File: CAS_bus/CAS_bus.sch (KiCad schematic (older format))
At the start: 2 parts

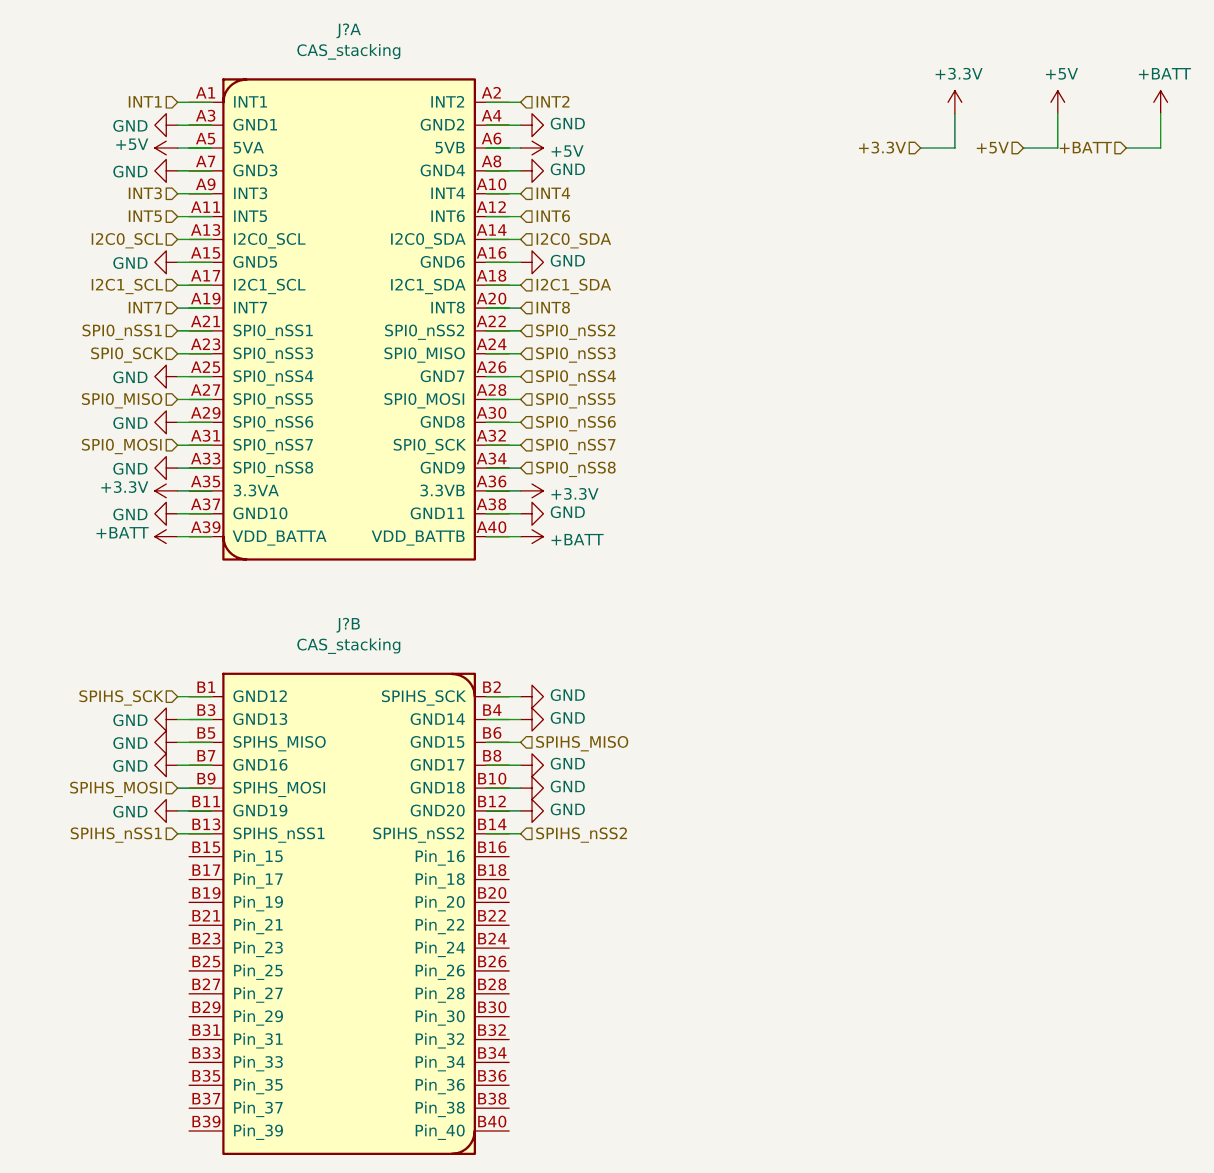
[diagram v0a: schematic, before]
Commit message: flip both connectors to match spreadsheet, and add pin names
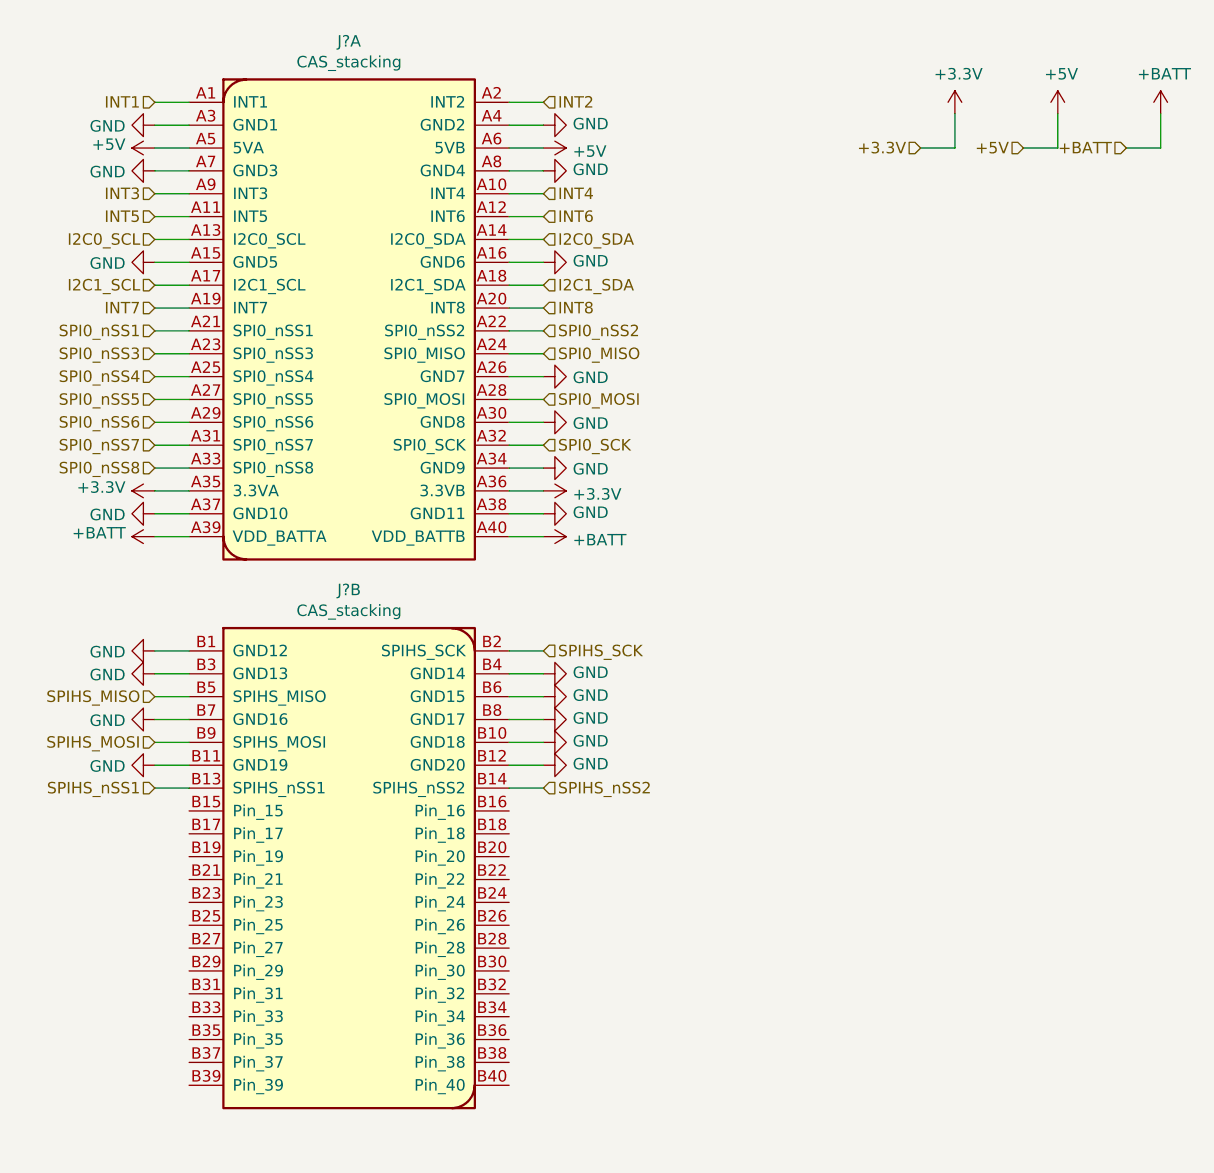
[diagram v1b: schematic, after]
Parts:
- removed J? (x2): CAS_stacking, symbol star-common-lib:CAS_stacking
- added J? (x2): CAS_stacking, symbol star-sch-block-symbols:CAS_stacking

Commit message: fix spelling error
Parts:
- removed J? (x2): CAS_stacking, symbol star-sch-block-symbols:CAS_stacking
- added J? (x2): CAS_stacking, symbol star-sch-block-symbols:CAS_stacking
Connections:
- net +3V3: now also J?.A35 (3.3VA), J?.A36 (3.3VB)
- net +5V: now also J?.A5 (5VA), J?.A6 (5VB)
- net +BATT: now also J?.A39 (VDD_BATTA), J?.A40 (VDD_BATTB)
- net GND: now also J?.A15 (GND5), J?.A16 (GND6), J?.A26 (GND7), J?.A3 (GND1), J?.A30 (GND8), J?.A34 (GND9), J?.A37 (GND10), J?.A38 (GND11), J?.A4 (GND2), J?.A7 (GND3), J?.A8 (GND4), J?.B1 (GND12), J?.B10 (GND18), J?.B11 (GND19), J?.B12 (GND20), J?.B3 (GND13), J?.B4 (GND14), J?.B6 (GND15), J?.B7 (GND16), J?.B8 (GND17)
- net I2C0_SCL: now also J?.A13 (I2C0_SCL)
- net I2C0_SDA: now also J?.A14 (I2C0_SDA)
- net I2C1_SCL: now also J?.A17 (I2C1_SCL)
- net I2C1_SDA: now also J?.A18 (I2C1_SDA)
- net INT1: now also J?.A1 (INT1)
- net INT2: now also J?.A2 (INT2)
- net INT3: now also J?.A9 (INT3)
- net INT4: now also J?.A10 (INT4)
- net INT5: now also J?.A11 (INT5)
- net INT6: now also J?.A12 (INT6)
- net INT7: now also J?.A19 (INT7)
- net INT8: now also J?.A20 (INT8)
- net SPI0_MISO: now also J?.A24 (SPI0_MISO)
- net SPI0_MOSI: now also J?.A28 (SPI0_MOSI)
- net SPI0_SCK: now also J?.A32 (SPI0_SCK)
- net SPI0_nSS1: now also J?.A21 (SPI0_nSS1)
- net SPI0_nSS2: now also J?.A22 (SPI0_nSS2)
- net SPI0_nSS3: now also J?.A23 (SPI0_nSS3)
- net SPI0_nSS4: now also J?.A25 (SPI0_nSS4)
- net SPI0_nSS5: now also J?.A27 (SPI0_nSS5)
- net SPI0_nSS6: now also J?.A29 (SPI0_nSS6)
- net SPI0_nSS7: now also J?.A31 (SPI0_nSS7)
- net SPI0_nSS8: now also J?.A33 (SPI0_nSS8)
- net SPIHS_MISO: now also J?.B5 (SPIHS_MISO)
- net SPIHS_MOSI: now also J?.B9 (SPIHS_MOSI)
- net SPIHS_SCK: now also J?.B2 (SPIHS_SCK)
- net SPIHS_nSS1: now also J?.B13 (SPIHS_nSS1)
- net SPIHS_nSS2: now also J?.B14 (SPIHS_nSS2)
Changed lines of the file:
@@
 Wire Wire Line
 	8700 2000 8700 1850
-$Comp
-L star-sch-block-symbols:CAS_stacking J?
-U 1 1 5EF11983
-P 5150 2750
-F 0 "J?" H 5150 3967 50  0000 C CNN
-F 1 "CAS_stacking" H 5150 3876 50  0000 C CNN
-F 2 "" H 5250 3700 50  0001 C CNN
-F 3 "" H 5250 3700 50  0001 C CNN
-	1    5150 2750
-	1    0    0    -1
-$EndComp
-$Comp
-L star-sch-block-symbols:CAS_stacking J?
-U 2 1 5EF130AD
-P 5150 5150
-F 0 "J?" H 5150 6367 50  0000 C CNN
-F 1 "CAS_stacking" H 5150 6276 50  0000 C CNN
-F 2 "" H 5250 6100 50  0001 C CNN
-F 3 "" H 5250 6100 50  0001 C CNN
-	2    5150 5150
-	1    0    0    -1
-$EndComp
 Wire Wire Line
 	4300 3500 4450 3500
@@
 Text HLabel 4300 2800 0    50   Input ~ 0
 SPI0_nSS1
+$Comp
+L star-sch-block-symbols:CAS_stacking J?
+U 1 1 5EF72F3E
+P 5150 2750
+F 0 "J?" H 5150 3967 50  0000 C CNN
+F 1 "CAS_stacking" H 5150 3876 50  0000 C CNN
+F 2 "" H 5250 3700 50  0001 C CNN
+F 3 "" H 5250 3700 50  0001 C CNN
+	1    5150 2750
+	1    0    0    -1
+$EndComp
+$Comp
+L star-sch-block-symbols:CAS_stacking J?
+U 2 1 5EF77901
+P 5150 5150
+F 0 "J?" H 5150 6367 50  0000 C CNN
+F 1 "CAS_stacking" H 5150 6276 50  0000 C CNN
+F 2 "" H 5250 6100 50  0001 C CNN
+F 3 "" H 5250 6100 50  0001 C CNN
+	2    5150 5150
+	1    0    0    -1
+$EndComp
 $EndSCHEMATC

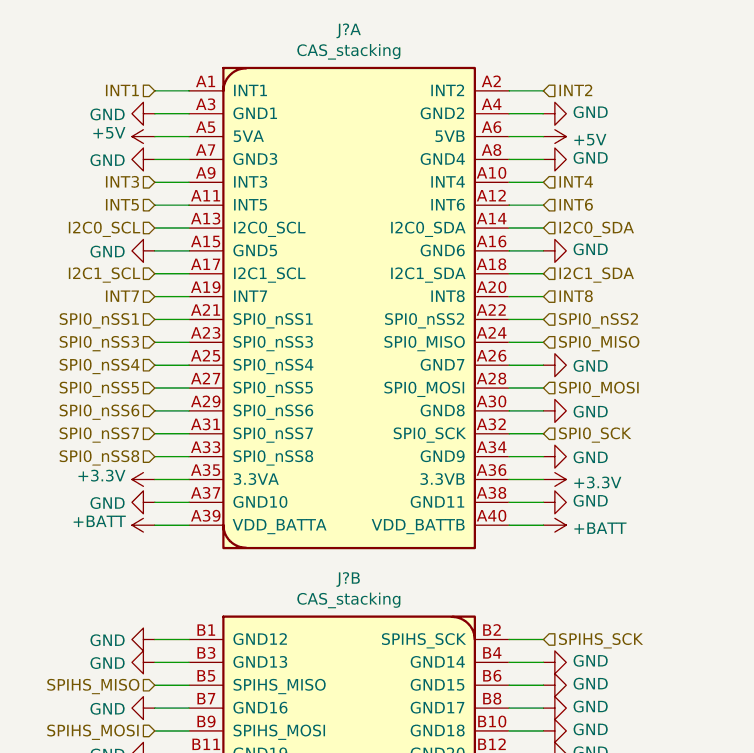
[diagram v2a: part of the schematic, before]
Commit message: fix some relative paths
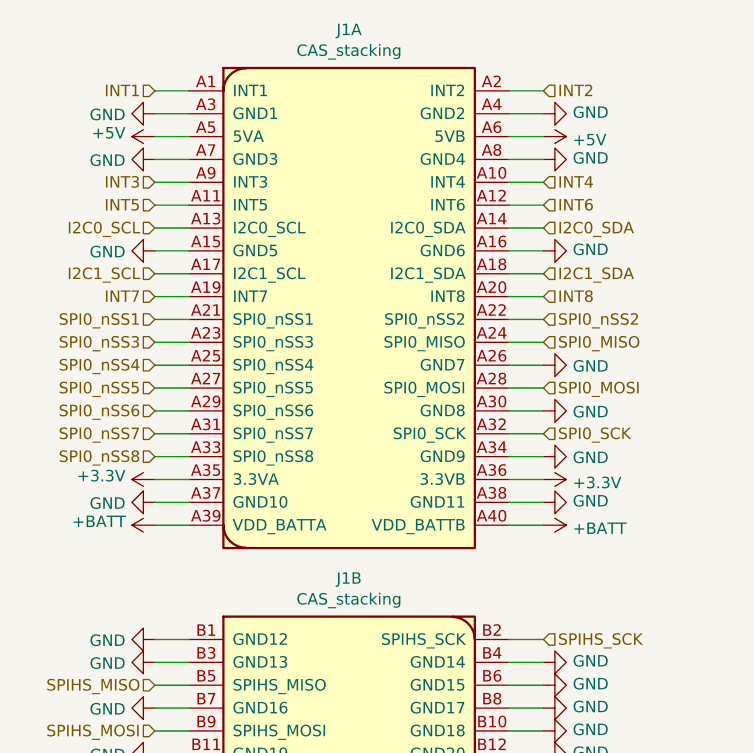
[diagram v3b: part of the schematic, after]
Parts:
- removed J? (x2): CAS_stacking, symbol star-sch-block-symbols:CAS_stacking
- added J1: CAS_stacking, symbol star-common-lib:CAS_stacking
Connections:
- net +3V3: now also J1.A35 (3.3VA), J1.A36 (3.3VB)
- net +5V: now also J1.A5 (5VA), J1.A6 (5VB)
- net +BATT: now also J1.A39 (VDD_BATTA), J1.A40 (VDD_BATTB)
- net GND: now also J1.A15 (GND5), J1.A16 (GND6), J1.A26 (GND7), J1.A3 (GND1), J1.A30 (GND8), J1.A34 (GND9), J1.A37 (GND10), J1.A38 (GND11), J1.A4 (GND2), J1.A7 (GND3), J1.A8 (GND4), J1.B1 (GND12), J1.B10 (GND18), J1.B11 (GND19), J1.B12 (GND20), J1.B3 (GND13), J1.B4 (GND14), J1.B6 (GND15), J1.B7 (GND16), J1.B8 (GND17)
- net I2C0_SCL: now also J1.A13 (I2C0_SCL)
- net I2C0_SDA: now also J1.A14 (I2C0_SDA)
- net I2C1_SCL: now also J1.A17 (I2C1_SCL)
- net I2C1_SDA: now also J1.A18 (I2C1_SDA)
- net INT1: now also J1.A1 (INT1)
- net INT2: now also J1.A2 (INT2)
- net INT3: now also J1.A9 (INT3)
- net INT4: now also J1.A10 (INT4)
- net INT5: now also J1.A11 (INT5)
- net INT6: now also J1.A12 (INT6)
- net INT7: now also J1.A19 (INT7)
- net INT8: now also J1.A20 (INT8)
- net SPI0_MISO: now also J1.A24 (SPI0_MISO)
- net SPI0_MOSI: now also J1.A28 (SPI0_MOSI)
- net SPI0_SCK: now also J1.A32 (SPI0_SCK)
- net SPI0_nSS1: now also J1.A21 (SPI0_nSS1)
- net SPI0_nSS2: now also J1.A22 (SPI0_nSS2)
- net SPI0_nSS3: now also J1.A23 (SPI0_nSS3)
- net SPI0_nSS4: now also J1.A25 (SPI0_nSS4)
- net SPI0_nSS5: now also J1.A27 (SPI0_nSS5)
- net SPI0_nSS6: now also J1.A29 (SPI0_nSS6)
- net SPI0_nSS7: now also J1.A31 (SPI0_nSS7)
- net SPI0_nSS8: now also J1.A33 (SPI0_nSS8)
- net SPIHS_MISO: now also J1.B5 (SPIHS_MISO)
- net SPIHS_MOSI: now also J1.B9 (SPIHS_MOSI)
- net SPIHS_SCK: now also J1.B2 (SPIHS_SCK)
- net SPIHS_nSS1: now also J1.B13 (SPIHS_nSS1)
- net SPIHS_nSS2: now also J1.B14 (SPIHS_nSS2)
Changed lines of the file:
@@
 SPI0_nSS8
 $Comp
-L power:+5V #PWR?
+L power:+5V #PWR02
 U 1 1 5EAFC0A6
 P 4300 2000
-F 0 "#PWR?" H 4300 1850 50  0001 C CNN
+F 0 "#PWR02" H 4300 1850 50  0001 C CNN
 F 1 "+5V" V 4315 2128 50  0000 L CNN
 F 2 "" H 4300 2000 50  0001 C CNN
@@
 $EndComp
 $Comp
-L power:+5V #PWR?
+L power:+5V #PWR013
 U 1 1 5EAFC439
 P 6000 2000
-F 0 "#PWR?" H 6000 1850 50  0001 C CNN
+F 0 "#PWR013" H 6000 1850 50  0001 C CNN
 F 1 "+5V" V 6015 2128 50  0000 L CNN
 F 2 "" H 6000 2000 50  0001 C CNN
@@
 $EndComp
 $Comp
-L power:+3.3V #PWR?
+L power:+3.3V #PWR019
 U 1 1 5EAFC7C9
 P 6000 3500
-F 0 "#PWR?" H 6000 3350 50  0001 C CNN
+F 0 "#PWR019" H 6000 3350 50  0001 C CNN
 F 1 "+3.3V" V 6015 3628 50  0000 L CNN
 F 2 "" H 6000 3500 50  0001 C CNN
@@
 $EndComp
 $Comp
-L power:+BATT #PWR?
+L power:+BATT #PWR07
 U 1 1 5EAFCF46
 P 4300 3700
-F 0 "#PWR?" H 4300 3550 50  0001 C CNN
+F 0 "#PWR07" H 4300 3550 50  0001 C CNN
 F 1 "+BATT" V 4315 3827 50  0000 L CNN
 F 2 "" H 4300 3700 50  0001 C CNN
@@
 $EndComp
 $Comp
-L power:+BATT #PWR?
+L power:+BATT #PWR021
 U 1 1 5EAFD5BD
 P 6000 3700
-F 0 "#PWR?" H 6000 3550 50  0001 C CNN
+F 0 "#PWR021" H 6000 3550 50  0001 C CNN
 F 1 "+BATT" V 6015 3828 50  0000 L CNN
 F 2 "" H 6000 3700 50  0001 C CNN
@@
 $EndComp
 $Comp
-L power:GND #PWR?
+L power:GND #PWR015
 U 1 1 5EAFD991
 P 6000 2500
-F 0 "#PWR?" H 6000 2250 50  0001 C CNN
+F 0 "#PWR015" H 6000 2250 50  0001 C CNN
 F 1 "GND" V 6005 2372 50  0000 R CNN
 F 2 "" H 6000 2500 50  0001 C CNN
@@
 $EndComp
 $Comp
-L power:GND #PWR?
+L power:GND #PWR04
 U 1 1 5EAFDD6C
 P 4300 2500
-F 0 "#PWR?" H 4300 2250 50  0001 C CNN
+F 0 "#PWR04" H 4300 2250 50  0001 C CNN
 F 1 "GND" V 4305 2372 50  0000 R CNN
 F 2 "" H 4300 2500 50  0001 C CNN
@@
 $EndComp
 $Comp
-L power:GND #PWR?
+L power:GND #PWR020
 U 1 1 5EAFEFF0
 P 6000 3600
-F 0 "#PWR?" H 6000 3350 50  0001 C CNN
+F 0 "#PWR020" H 6000 3350 50  0001 C CNN
 F 1 "GND" V 6005 3472 50  0000 R CNN
 F 2 "" H 6000 3600 50  0001 C CNN
@@
 	5850 2000 6000 2000
 $Comp
-L power:GND #PWR?
+L power:GND #PWR012
 U 1 1 5EB0043E
 P 6000 1900
-F 0 "#PWR?" H 6000 1650 50  0001 C CNN
+F 0 "#PWR012" H 6000 1650 50  0001 C CNN
 F 1 "GND" V 6005 1772 50  0000 R CNN
 F 2 "" H 6000 1900 50  0001 C CNN
@@
 $EndComp
 $Comp
-L power:GND #PWR?
+L power:GND #PWR014
 U 1 1 5EB00872
 P 6000 2100
-F 0 "#PWR?" H 6000 1850 50  0001 C CNN
+F 0 "#PWR014" H 6000 1850 50  0001 C CNN
 F 1 "GND" V 6005 1972 50  0000 R CNN
 F 2 "" H 6000 2100 50  0001 C CNN
@@
 $EndComp
 $Comp
-L power:GND #PWR?
+L power:GND #PWR01
 U 1 1 5EB00CA1
 P 4300 1900
-F 0 "#PWR?" H 4300 1650 50  0001 C CNN
+F 0 "#PWR01" H 4300 1650 50  0001 C CNN
 F 1 "GND" V 4305 1772 50  0000 R CNN
 F 2 "" H 4300 1900 50  0001 C CNN
@@
 $EndComp
 $Comp
-L power:GND #PWR?
+L power:GND #PWR03
 U 1 1 5EB01123
 P 4300 2100
-F 0 "#PWR?" H 4300 1850 50  0001 C CNN
+F 0 "#PWR03" H 4300 1850 50  0001 C CNN
 F 1 "GND" V 4305 1972 50  0000 R CNN
 F 2 "" H 4300 2100 50  0001 C CNN
@@
 SPIHS_nSS2
 $Comp
-L power:GND #PWR?
+L power:GND #PWR08
 U 1 1 5EB1964E
 P 4300 4200
-F 0 "#PWR?" H 4300 3950 50  0001 C CNN
+F 0 "#PWR08" H 4300 3950 50  0001 C CNN
 F 1 "GND" V 4305 4072 50  0000 R CNN
 F 2 "" H 4300 4200 50  0001 C CNN
@@
 $EndComp
 $Comp
-L power:GND #PWR?
+L power:GND #PWR09
 U 1 1 5EB19A77
 P 4300 4300
-F 0 "#PWR?" H 4300 4050 50  0001 C CNN
+F 0 "#PWR09" H 4300 4050 50  0001 C CNN
 F 1 "GND" V 4305 4172 50  0000 R CNN
 F 2 "" H 4300 4300 50  0001 C CNN
@@
 $EndComp
 $Comp
-L power:GND #PWR?
+L power:GND #PWR010
 U 1 1 5EB19EAC
 P 4300 4500
-F 0 "#PWR?" H 4300 4250 50  0001 C CNN
+F 0 "#PWR010" H 4300 4250 50  0001 C CNN
 F 1 "GND" V 4305 4372 50  0000 R CNN
 F 2 "" H 4300 4500 50  0001 C CNN
@@
 $EndComp
 $Comp
-L power:GND #PWR?
+L power:GND #PWR011
 U 1 1 5EB1A2ED
 P 4300 4700
-F 0 "#PWR?" H 4300 4450 50  0001 C CNN
+F 0 "#PWR011" H 4300 4450 50  0001 C CNN
 F 1 "GND" V 4305 4572 50  0000 R CNN
 F 2 "" H 4300 4700 50  0001 C CNN
@@
 $EndComp
 $Comp
-L power:GND #PWR?
+L power:GND #PWR022
 U 1 1 5EB1A73A
 P 6000 4300
-F 0 "#PWR?" H 6000 4050 50  0001 C CNN
+F 0 "#PWR022" H 6000 4050 50  0001 C CNN
 F 1 "GND" V 6005 4172 50  0000 R CNN
 F 2 "" H 6000 4300 50  0001 C CNN
@@
 $EndComp
 $Comp
-L power:GND #PWR?
+L power:GND #PWR023
 U 1 1 5EB1ABC9
 P 6000 4400
-F 0 "#PWR?" H 6000 4150 50  0001 C CNN
+F 0 "#PWR023" H 6000 4150 50  0001 C CNN
 F 1 "GND" V 6005 4272 50  0000 R CNN
 F 2 "" H 6000 4400 50  0001 C CNN
@@
 $EndComp
 $Comp
-L power:GND #PWR?
+L power:GND #PWR024
 U 1 1 5EB1B064
 P 6000 4500
-F 0 "#PWR?" H 6000 4250 50  0001 C CNN
+F 0 "#PWR024" H 6000 4250 50  0001 C CNN
 F 1 "GND" V 6005 4372 50  0000 R CNN
 F 2 "" H 6000 4500 50  0001 C CNN
@@
 $EndComp
 $Comp
-L power:GND #PWR?
+L power:GND #PWR025
 U 1 1 5EB1B50B
 P 6000 4600
-F 0 "#PWR?" H 6000 4350 50  0001 C CNN
+F 0 "#PWR025" H 6000 4350 50  0001 C CNN
 F 1 "GND" V 6005 4472 50  0000 R CNN
 F 2 "" H 6000 4600 50  0001 C CNN
@@
 $EndComp
 $Comp
-L power:GND #PWR?
+L power:GND #PWR026
 U 1 1 5EB1B9BE
 P 6000 4700
-F 0 "#PWR?" H 6000 4450 50  0001 C CNN
+F 0 "#PWR026" H 6000 4450 50  0001 C CNN
 F 1 "GND" V 6005 4572 50  0000 R CNN
 F 2 "" H 6000 4700 50  0001 C CNN
@@
 +3.3V
 $Comp
-L power:+3.3V #PWR?
+L power:+3.3V #PWR027
 U 1 1 5EB35B08
 P 7800 1850
-F 0 "#PWR?" H 7800 1700 50  0001 C CNN
+F 0 "#PWR027" H 7800 1700 50  0001 C CNN
 F 1 "+3.3V" H 7815 2023 50  0000 C CNN
 F 2 "" H 7800 1850 50  0001 C CNN
@@
 +BATT
 $Comp
-L power:+5V #PWR?
+L power:+5V #PWR028
 U 1 1 5EB368D5
 P 8250 1850
-F 0 "#PWR?" H 8250 1700 50  0001 C CNN
+F 0 "#PWR028" H 8250 1700 50  0001 C CNN
 F 1 "+5V" H 8265 2023 50  0000 C CNN
 F 2 "" H 8250 1850 50  0001 C CNN
@@
 $EndComp
 $Comp
-L power:+BATT #PWR?
+L power:+BATT #PWR029
 U 1 1 5EB37213
 P 8700 1850
-F 0 "#PWR?" H 8700 1700 50  0001 C CNN
+F 0 "#PWR029" H 8700 1700 50  0001 C CNN
 F 1 "+BATT" H 8715 2023 50  0000 C CNN
 F 2 "" H 8700 1850 50  0001 C CNN
@@
 	4300 2800 4450 2800
 $Comp
-L power:GND #PWR?
+L power:GND #PWR018
 U 1 1 5EB01534
 P 6000 3400
-F 0 "#PWR?" H 6000 3150 50  0001 C CNN
+F 0 "#PWR018" H 6000 3150 50  0001 C CNN
 F 1 "GND" V 6005 3272 50  0000 R CNN
 F 2 "" H 6000 3400 50  0001 C CNN
@@
 $EndComp
 $Comp
-L power:GND #PWR?
+L power:GND #PWR06
 U 1 1 5EAFEC1B
 P 4300 3600
-F 0 "#PWR?" H 4300 3350 50  0001 C CNN
+F 0 "#PWR06" H 4300 3350 50  0001 C CNN
 F 1 "GND" V 4305 3472 50  0000 R CNN
 F 2 "" H 4300 3600 50  0001 C CNN
@@
 $EndComp
 $Comp
-L power:GND #PWR?
+L power:GND #PWR017
 U 1 1 5EAFE4EB
 P 6000 3200
-F 0 "#PWR?" H 6000 2950 50  0001 C CNN
+F 0 "#PWR017" H 6000 2950 50  0001 C CNN
 F 1 "GND" V 6005 3072 50  0000 R CNN
 F 2 "" H 6000 3200 50  0001 C CNN
@@
 $EndComp
 $Comp
-L power:GND #PWR?
+L power:GND #PWR016
 U 1 1 5EAFE12E
 P 6000 3000
-F 0 "#PWR?" H 6000 2750 50  0001 C CNN
+F 0 "#PWR016" H 6000 2750 50  0001 C CNN
 F 1 "GND" V 6005 2872 50  0000 R CNN
 F 2 "" H 6000 3000 50  0001 C CNN
@@
 $EndComp
 $Comp
-L power:+3.3V #PWR?
+L power:+3.3V #PWR05
 U 1 1 5EAFCB48
 P 4300 3500
-F 0 "#PWR?" H 4300 3350 50  0001 C CNN
+F 0 "#PWR05" H 4300 3350 50  0001 C CNN
 F 1 "+3.3V" V 4315 3628 50  0000 L CNN
 F 2 "" H 4300 3500 50  0001 C CNN
@@
 SPI0_nSS1
 $Comp
-L star-sch-block-symbols:CAS_stacking J?
-U 1 1 5EF72F3E
+L star-common-lib:CAS_stacking J1
+U 1 1 5F2F934D
 P 5150 2750
-F 0 "J?" H 5150 3967 50  0000 C CNN
+F 0 "J1" H 5150 3967 50  0000 C CNN
 F 1 "CAS_stacking" H 5150 3876 50  0000 C CNN
 F 2 "" H 5250 3700 50  0001 C CNN
@@
 $EndComp
 $Comp
-L star-sch-block-symbols:CAS_stacking J?
-U 2 1 5EF77901
+L star-common-lib:CAS_stacking J1
+U 2 1 5F2FC6A4
 P 5150 5150
-F 0 "J?" H 5150 6367 50  0000 C CNN
+F 0 "J1" H 5150 6367 50  0000 C CNN
 F 1 "CAS_stacking" H 5150 6276 50  0000 C CNN
 F 2 "" H 5250 6100 50  0001 C CNN
